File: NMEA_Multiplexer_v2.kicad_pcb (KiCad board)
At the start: 2 copper layers, 65 x 45 mm, 94 parts, among them J1 USB, J2 PoRt 1, J3 PoRt 2, J4 PoRt 3, J5 PoRt 4, J6 PoRt 5, J7 12V, J8 DEBUG UART, J9 JTAG, SW1 Reset, U1 ATSAMG55J19A-AU, U2 XR32330, U3 XR32330, U4 LF33ABDT-TR, U5 HM-11, Y1 32.768k

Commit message: Soon complete
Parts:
- C11: value 100n -> 4.7u
- C12: value 4.7u -> 100n
- moved R1 9.80 mm to (226.6, 117.8), turned to 90 degrees
- moved R2 8.55 mm to (228.0, 117.8), turned to 90 degrees
- moved R3 7.62 mm to (229.4, 117.8), turned to 90 degrees
- moved R15 4.05 mm to (226.4, 127.6)
- moved R14 4.05 mm to (226.4, 126.2)
- moved C27 1.20 mm to (229.4, 141.8)
- moved C28 1.20 mm to (230.6, 141.8)
- renumbered R15 to R1, R7 to R10, R8 to R11, R9 to R12, R10 to R13, R11 to R14, R12 to R15, R14 to R2, R13 to R3, R1 to R4, R3 to R5, R2 to R6, R4 to R7, R5 to R8, R6 to R9
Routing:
- net GND: track 133.3 -> 159.8 mm, vias 47 -> 50
- net /RX3: track 0.00 -> 22.4 mm, vias 0 -> 2
- net /TX4: track 0.00 -> 22.1 mm, vias 0 -> 2
- net /TX3: track 0.00 -> 19.1 mm, vias 0 -> 2
- net /RX4: track 0.00 -> 17.5 mm, vias 0 -> 1
- net Net-(D1-Pad2): track 0.00 -> 15.3 mm
- net Net-(D4-Pad2): track 0.00 -> 14.1 mm
- net Net-(D2-Pad2): track 0.00 -> 13.6 mm
- net Net-(D3-Pad2): track 0.00 -> 9.96 mm
- net Net-(D5-Pad2): track 0.00 -> 9.95 mm
- net /LED_3_RX: track 4.81 -> 12.5 mm, vias 0 -> 2
- net Net-(D6-Pad2): track 0.00 -> 6.55 mm
- net /LED_3_ERR: track 5.19 -> 11.5 mm, vias 0 -> 2
- net /LED_3_TX: track 5.56 -> 10.4 mm, vias 0 -> 2
- net /VBUS_3.3V: track 10.4 -> 6.63 mm
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
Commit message: Everything connected!
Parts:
- moved C14 1.55 mm to (217.2, 129.8), turned to 0 degrees
- moved JP1 0.80 mm to (245.4, 122.4)
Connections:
- net /CxTS0 renamed /CTS0
- net /TCxK renamed /TCK
- U2 pad 1: /RX3 -> /RX4
- U2 pad 11: /RXD2 -> /RXD3
- U2 pad 12: /RXD3 -> /RXD2
- U2 pad 2: /RX4 -> /RX3
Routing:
- net +3V3: track 109.2 -> 226.5 mm, vias 5 -> 14
- net +1V8: track 18.3 -> 37.8 mm, vias 0 -> 2
- net GND: track 159.8 -> 174.9 mm, vias 50 -> 49
- net /TCK: track 20.5 -> 18.4 mm
- net Net-(JP1-Pad2): track 6.77 -> 5.04 mm, vias 1 -> 0
- net /TXD0: track 27.2 -> 26.6 mm
- net /RTS0: track 24.8 -> 24.2 mm
- net /RXD0: track 26.4 -> 25.9 mm
- net /RX3: track 22.4 -> 22.8 mm, vias 2 -> 0
- net Net-(C15-Pad1): vias 1 -> 2
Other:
- board text added: "(c)2017"
- board text added: "MN015"
- board text added: "MaxNil"
- board text added: "NMEA Mux. v2.0"

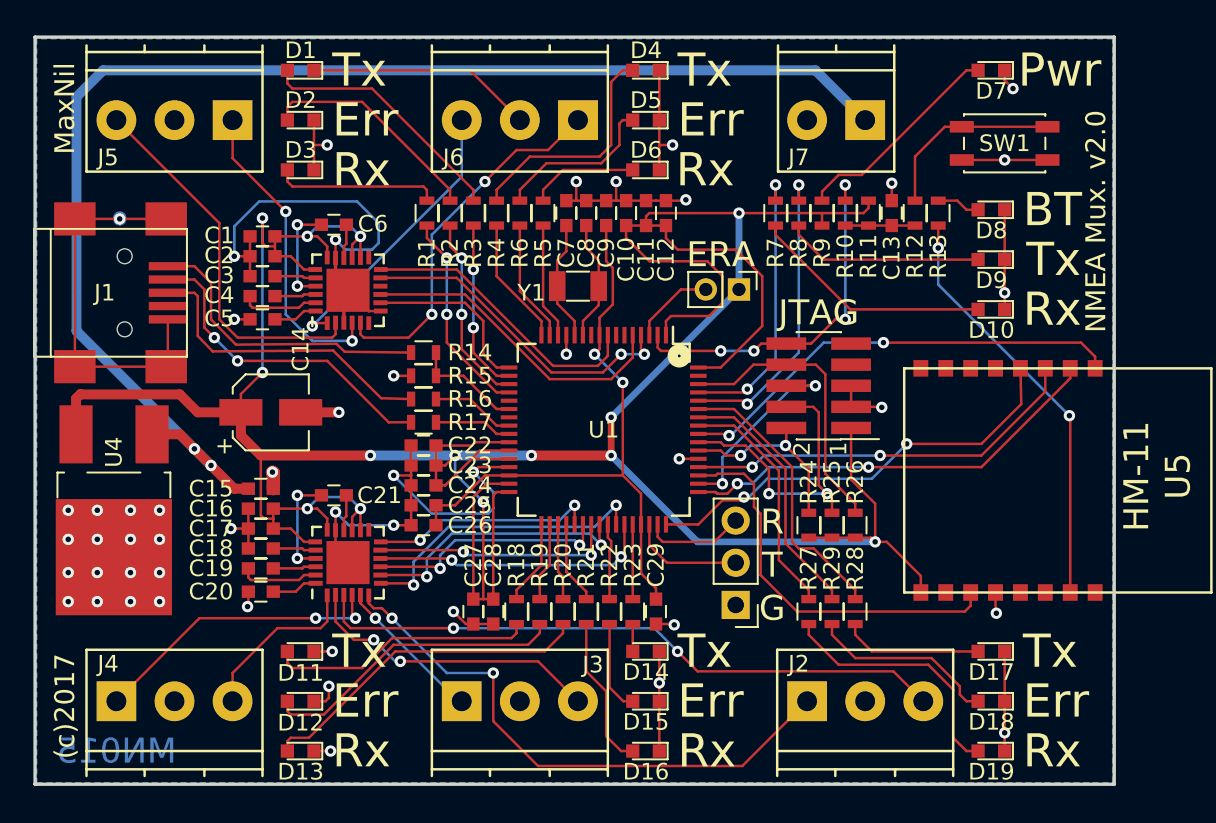
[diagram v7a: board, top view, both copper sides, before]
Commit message: Added copyright and board text
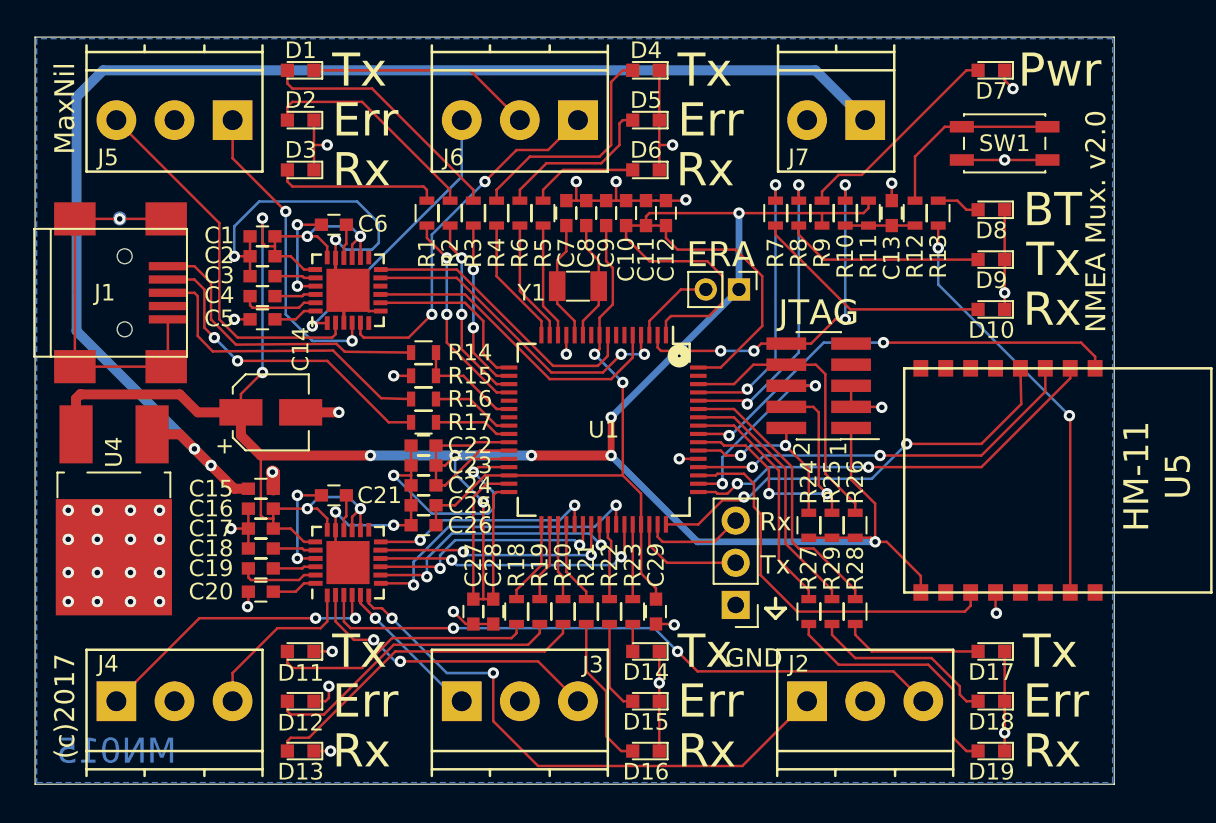
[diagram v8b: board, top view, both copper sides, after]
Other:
- board text added: "GND"
- board text removed: "G"
- board text removed: "R"
- board text removed: "T"
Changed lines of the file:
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@@
     (links 217)
     (no_connects 0)
-    (area 202.899999 107.099999 268.100001 152.300001)
+    (area 158.399999 90.399999 274.077401 179.700001)
     (thickness 1.6)
-    (drawings 41)
+    (drawings 45)
     (tracks 890)
     (zones 0)
@@
     (zone_45_only no)
     (trace_min 0.1524)
-    (segment_width 0.5)
-    (edge_width 0.2)
+    (segment_width 0.2)
+    (edge_width 0.01)
     (via_size 0.6858)
     (via_drill 0.3302)
@@
     )
   )
+  (gr_line (start 247.6 141.6) (end 247.6 141) (angle 90) (layer F.SilkS) (width 0.2))
+  (gr_line (start 248.2 141.6) (end 247 141.6) (angle 90) (layer F.SilkS) (width 0.2))
+  (gr_line (start 247.6 142.2) (end 248.2 141.6) (angle 90) (layer F.SilkS) (width 0.2))
+  (gr_line (start 247 141.6) (end 247.6 142.2) (angle 90) (layer F.SilkS) (width 0.2))
   (gr_text MaxNil (at 204.8 111.5 90) (layer F.SilkS)
     (effects (font (size 1.2 1.2) (thickness 0.3)))
@@
     (effects (font (size 1.5 1.5) (thickness 0.3)))
   )
-  (gr_text G (at 247.4 141.6) (layer F.SilkS)
-    (effects (font (size 1.5 1.5) (thickness 0.3)))
+  (gr_text GND (at 246.3 144.6) (layer F.SilkS)
+    (effects (font (size 1.1 1.1) (thickness 0.2)))
   )
-  (gr_text T (at 247.4 139) (layer F.SilkS)
-    (effects (font (size 1.5 1.5) (thickness 0.3)))
+  (gr_text Tx (at 247.6 139) (layer F.SilkS)
+    (effects (font (size 1.1 1.1) (thickness 0.2)))
   )
-  (gr_text R (at 247.4 136.4) (layer F.SilkS)
-    (effects (font (size 1.5 1.5) (thickness 0.3)))
+  (gr_text Rx (at 247.6 136.4) (layer F.SilkS)
+    (effects (font (size 1.1 1.1) (thickness 0.2)))
   )
   (gr_text 1 (at 251.4 132 90) (layer F.SilkS)
@@
   )
   (gr_circle (center 241.8 126.4) (end 241.8 126.7) (layer F.SilkS) (width 0.8))
-  (gr_line (start 268 107.2) (end 203 107.2) (angle 90) (layer Edge.Cuts) (width 0.2))
-  (gr_line (start 268 152.2) (end 268 107.2) (angle 90) (layer Edge.Cuts) (width 0.2))
-  (gr_line (start 203 152.2) (end 268 152.2) (angle 90) (layer Edge.Cuts) (width 0.2))
-  (gr_line (start 203 107.2) (end 203 152.2) (angle 90) (layer Edge.Cuts) (width 0.2))
+  (gr_line (start 268 107.2) (end 203 107.2) (angle 90) (layer Edge.Cuts) (width 0.01))
+  (gr_line (start 268 152.2) (end 268 107.2) (angle 90) (layer Edge.Cuts) (width 0.01))
+  (gr_line (start 203 152.2) (end 268 152.2) (angle 90) (layer Edge.Cuts) (width 0.01))
+  (gr_line (start 203 107.2) (end 203 152.2) (angle 90) (layer Edge.Cuts) (width 0.01))
   (gr_text BT (at 262.5 117.6) (layer F.SilkS)
     (effects (font (size 2 2) (thickness 0.3)) (justify left))
